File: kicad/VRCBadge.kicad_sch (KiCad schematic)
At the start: 0 parts

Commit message: feat: add power, peripheral schematics and custom component libraries
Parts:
- added C12, C17, C19, C20, C22: 100nF, symbol Device:C
- added C13, C14, C21: 1uF, symbol Device:C
- added C15, C16, C18: 10uF, symbol Device:C
- added D3, D4: LED_R, symbol Device:LED
- added J4: Conn_01x02, symbol Connector_Generic:Conn_01x02
- added J5: USB_C_Receptacle_USB2.0_16P, symbol Connector:USB_C_Receptacle_USB2.0_16P
- added J6: Conn_01x13_Socket, symbol Connector:Conn_01x13_Socket
- added Q2: FS8205A, Package_TO_SOT_SMD:SOT-23-6, symbol VRCBadge:FS8205A
- added R11, R12: 5.1k, symbol Device:R
- added R13, R14: 1k, symbol Device:R
- added R15: 1.2k, symbol Device:R
- added R16, R17, R18: 10k, symbol Device:R
- added R19, R20: 4.7k, symbol Device:R
- added SW3: RESET, symbol Switch:SW_Push
- added SW4: BOOT, symbol Switch:SW_Push
- added U10: MAX17048G+T10, VRCBadge:TDFN-8_L2.0-W2.0-P0.50-BL-EP1.2, symbol VRCBadge:MAX17048G+T10
- added U6: DW01A, Package_TO_SOT_SMD:SOT-23-6, symbol Battery_Management:DW01A
- added U7: ME6211C33M5, Package_TO_SOT_SMD:SOT-23-5, symbol Regulator_Linear:ME6211C33M5
- added U8: TP4056-42-ESOP8, Package_SO:SOIC-8-1EP_3.9x4.9mm_P1.27mm_EP2.41x3.3mm_ThermalVias, symbol Battery_Management:TP4056-42-ESOP8
- added U9: ESP32-S3-WROOM-1U, RF_Module:ESP32-S3-WROOM-1U, symbol RF_Module:ESP32-S3-WROOM-1
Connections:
- new net: J5.A5 (CC1), R12.1
- new net: J5.B5 (CC2), R11.1
- new net: D4.1 (K), R14.1
- new net: D4.2 (A), U8.6 (~{STDBY})
- new net: D3.1 (K), R13.1
- new net: D3.2 (A), U8.7 (~{CHRG})
- new net: C21.1, U10.1 (CTG)
- new net: C22.2, U10.3 (VDD)
- new net: R15.2, U8.2 (PROG)
- new net: Q2.2 (D), Q2.5 (D)
- new net: R16.2, U8.1 (TEMP)
- new net +3V3: C14.1, C18.1, C19.1, C20.1, C22.1, J6.13 (Pin_13), R17.1, R18.1, R19.1, R20.1, U10.2 (CELL), U7.5 (V_{OUT}), U9.2 (3V3)
- new net +BATT: C12.2, C13.1, C16.1, J4.1 (Pin_1), U6.5 (VCC), U7.1 (V_{IN}), U7.3 (CE), U8.5 (BAT)
- new net -BATT: J4.2 (Pin_2), Q2.3 (S)
- new net CS: C12.1, Q2.1 (S), U6.2 (CS), U6.6 (GND)
- new net ESP_BOOT: R18.2, SW4.2, U9.27 (IO0)
- new net ESP_EN: C17.1, R17.2, SW3.1, U9.3 (EN)
- new net GND: C13.2, C14.2, C15.2, C16.2, C17.2, C18.2, C19.2, C20.2, C21.2, J5.A1 (GND), J5.A12 (GND), J5.B1 (GND), J5.B12 (GND), J5.S1 (SHIELD), J6.12 (Pin_12), R11.2, R12.2, R15.1, R16.1, SW3.2, SW4.1, U10.4 (GND), U10.9 (EP), U7.2 (V_{SS}), U8.3 (GND), U8.9 (EPAD), U9.1 (GND), U9.40 (GND), U9.41 (GND)
- new net I2C_SCL: J6.3 (Pin_3), R19.2, U10.7 (SCL), U9.38 (IO2)
- new net I2C_SDA: J6.4 (Pin_4), R20.2, U10.8 (SDA), U9.39 (IO1)
- new net LCD_BL: J6.5 (Pin_5), U9.7 (IO7)
- new net LCD_CS: J6.8 (Pin_8), U9.18 (IO10)
- new net LCD_DC: J6.7 (Pin_7), U9.17 (IO9)
- new net LCD_MISO: J6.11 (Pin_11), U9.21 (IO13)
- new net LCD_MOSI: J6.10 (Pin_10), U9.19 (IO11)
- new net LCD_RST: J6.6 (Pin_6), U9.12 (IO8)
- new net LCD_SCLK: J6.9 (Pin_9), U9.20 (IO12)
- new net OC: Q2.4 (G), U6.3 (OC)
- new net OD: Q2.6 (G), U6.1 (OD)
- new net TP_INT: J6.2 (Pin_2), U9.15 (IO3)
- new net TP_RST: J6.1 (Pin_1), U9.4 (IO4)
- new net USB_DN: J5.A7 (D-), J5.B7 (D-), U9.13 (USB_D-)
- new net USB_DP: J5.A6 (D+), J5.B6 (D+), U9.14 (USB_D+)
- new net VBUS: C15.1, J5.A4 (VBUS), J5.A9 (VBUS), J5.B4 (VBUS), J5.B9 (VBUS), R13.2, R14.2, U8.4 (V_{CC}), U8.8 (CE)
- no-connect marks 0 -> 24
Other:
- added sheet mcu (mcu.kicad_sch)
- added sheet peripheral (peripheral.kicad_sch)
- added sheet power (power.kicad_sch)

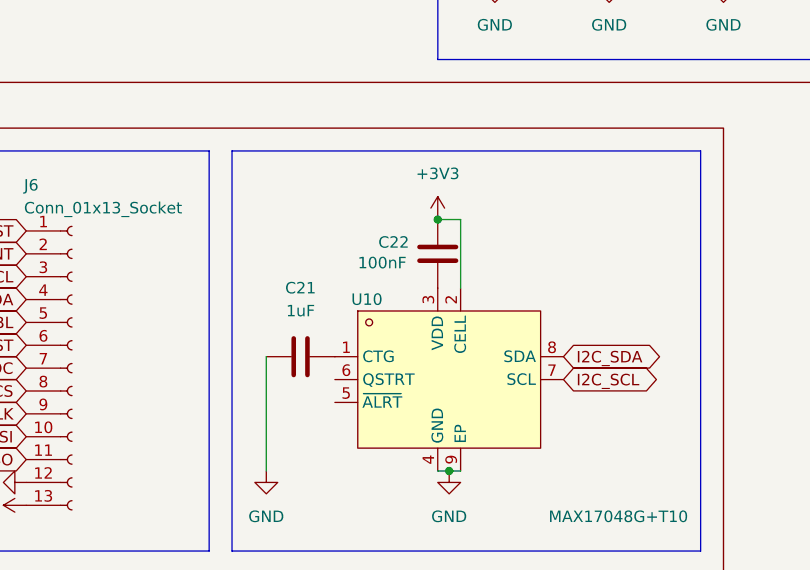
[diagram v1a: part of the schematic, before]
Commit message: feat: assign footprints and add no_connect flags for PCB readiness
- Assign footprints to 28 root-sheet components (0603 passives,
  0805 for 10uF, TL3342 switches, HRO USB-C, JST-PH/GH connectors)
- Add no_connect flags to MAX17048 ALRT and QSTRT pins
- Rewire MAX17048 CELL pin from +3V3 to +BATT on root sheet
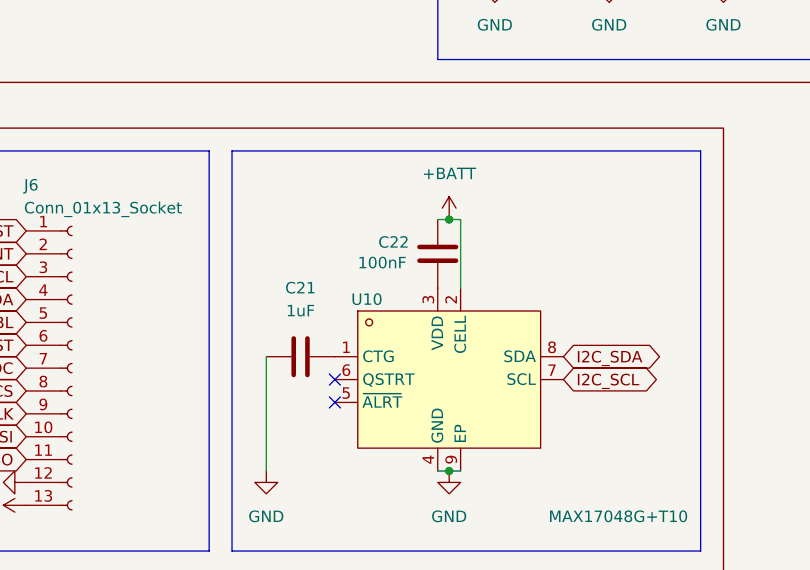
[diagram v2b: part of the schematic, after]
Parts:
- C12, C13, C14, C17, C19, C20, C21, C22: footprint (none) -> Capacitor_SMD:C_0603_1608Metric
- C15, C16, C18: footprint (none) -> Capacitor_SMD:C_0805_2012Metric
- D3, D4: footprint (none) -> LED_SMD:LED_0603_1608Metric
- J4: footprint (none) -> Connector_JST:JST_PH_S2B-PH-K_1x02_P2.00mm_Horizontal
- J5: footprint (none) -> Connector_USB:USB_C_Receptacle_HRO_TYPE-C-31-M-12
- J6: footprint (none) -> Connector_JST:JST_GH_SM13B-GHS-TB_1x13-1MP_P1.25mm_Horizontal
- R11, R12, R13, R14, R15, R16, R17, R18, R19, R20: footprint (none) -> Resistor_SMD:R_0603_1608Metric
- SW3, SW4: footprint (none) -> Button_Switch_SMD:SW_SPST_TL3342
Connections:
- net +3V3: no longer C22.1, U10.2 (CELL)
- net +BATT: now also C22.1, U10.2 (CELL)
- no-connect marks 24 -> 26
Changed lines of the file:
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@@
 	)
 	(junction
-		(at 255.27 147.32)
+		(at 256.54 147.32)
 		(diameter 0)
 		(color 0 0 0 0)
@@
 	)
 	(no_connect
+		(at 243.84 165.1)
+	)
+	(no_connect
 		(at 207.01 78.74)
 	)
@@
 	)
 	(no_connect
+		(at 243.84 167.64)
+	)
+	(no_connect
 		(at 237.49 55.88)
 	)
@@
 	(wire
 		(pts
+			(xy 256.54 147.32) (xy 255.27 147.32)
+		)
+		(stroke
+			(width 0)
+			(type default)
+		)
+	)
+	(wire
+		(pts
 			(xy 95.25 63.5) (xy 95.25 66.04)
 		)
@@
 	(wire
 		(pts
-			(xy 257.81 147.32) (xy 255.27 147.32)
+			(xy 257.81 147.32) (xy 256.54 147.32)
 		)
 		(stroke
@@
 			)
 		)
-		(property "Footprint" ""
+		(property "Footprint" "Resistor_SMD:R_0603_1608Metric"
 			(at 308.102 31.75 90)
 			(effects
@@
 			)
 		)
-		(property "Footprint" ""
+		(property "Footprint" "Connector_USB:USB_C_Receptacle_HRO_TYPE-C-31-M-12"
 			(at 39.37 45.72 0)
 			(effects
@@
 			)
 		)
-		(property "Footprint" ""
+		(property "Footprint" "Resistor_SMD:R_0603_1608Metric"
 			(at 64.262 41.91 90)
 			(effects
@@
 			)
 		)
-		(property "Footprint" ""
+		(property "Footprint" "LED_SMD:LED_0603_1608Metric"
 			(at 105.41 49.53 0)
 			(effects
@@
 			)
 		)
-		(property "Footprint" ""
+		(property "Footprint" "Connector_JST:JST_GH_SM13B-GHS-TB_1x13-1MP_P1.25mm_Horizontal"
 			(at 214.63 163.83 0)
 			(effects
@@
 			)
 		)
-		(property "Footprint" ""
+		(property "Footprint" "LED_SMD:LED_0603_1608Metric"
 			(at 95.25 49.53 0)
 			(effects
@@
 			)
 		)
-		(property "Footprint" ""
+		(property "Footprint" "Capacitor_SMD:C_0805_2012Metric"
 			(at 262.5852 120.65 0)
 			(effects
@@
 			)
 		)
-		(property "Footprint" ""
+		(property "Footprint" "Resistor_SMD:R_0603_1608Metric"
 			(at 316.992 31.75 90)
 			(effects
@@
 			)
 		)
-		(property "Footprint" ""
+		(property "Footprint" "Capacitor_SMD:C_0603_1608Metric"
 			(at 275.2852 93.98 0)
 			(effects
@@
 			)
 		)
-		(property "Footprint" ""
+		(property "Footprint" "Capacitor_SMD:C_0603_1608Metric"
 			(at 145.7452 101.6 0)
 			(effects
@@
 			)
 		)
-		(property "Footprint" ""
+		(property "Footprint" "Capacitor_SMD:C_0603_1608Metric"
 			(at 236.22 163.5252 0)
 			(effects
@@
 			)
 		)
-		(property "Footprint" ""
+		(property "Footprint" "Resistor_SMD:R_0603_1608Metric"
 			(at 142.748 49.53 90)
 			(effects
@@
 			)
 		)
-		(property "Footprint" ""
+		(property "Footprint" "Resistor_SMD:R_0603_1608Metric"
 			(at 71.882 41.91 90)
 			(effects
@@
 			)
 		)
-		(property "Footprint" ""
+		(property "Footprint" "Button_Switch_SMD:SW_SPST_TL3342"
 			(at 288.29 88.9 0)
 			(effects
@@
 			)
 		)
-		(property "Footprint" ""
+		(property "Footprint" "Capacitor_SMD:C_0603_1608Metric"
 			(at 256.2352 154.94 0)
 			(effects
@@
 			)
 		)
-		(property "Footprint" ""
+		(property "Footprint" "Connector_JST:JST_PH_S2B-PH-K_1x02_P2.00mm_Horizontal"
 			(at 24.13 92.71 0)
 			(effects
@@
 			)
 		)
-		(property "Footprint" ""
+		(property "Footprint" "Resistor_SMD:R_0603_1608Metric"
 			(at 275.082 33.02 90)
 			(effects
@@
 			)
 		)
-		(property "Footprint" ""
+		(property "Footprint" "Capacitor_SMD:C_0603_1608Metric"
 			(at 287.9852 120.65 0)
 			(effects
@@
 			)
 		)
-		(property "Footprint" ""
+		(property "Footprint" "Resistor_SMD:R_0603_1608Metric"
 			(at 272.542 74.93 90)
 			(effects
@@
 			)
 		)
-		(property "Footprint" ""
+		(property "Footprint" "Capacitor_SMD:C_0805_2012Metric"
 			(at 160.9852 52.07 0)
 			(effects
@@
 	)
 	(symbol
+		(lib_id "power:+BATT")
+		(at 256.54 147.32 0)
+		(unit 1)
+		(exclude_from_sim no)
+		(in_bom yes)
+		(on_board yes)
+		(dnp no)
+		(fields_autoplaced yes)
+		(property "Reference" "#PWR078"
+			(at 256.54 151.13 0)
+			(effects
+				(font
+					(size 1.27 1.27)
+				)
+				(hide yes)
+			)
+		)
+		(property "Value" "+BATT"
+			(at 256.54 142.24 0)
+			(effects
+				(font
+					(size 1.27 1.27)
+				)
+			)
+		)
+		(property "Footprint" ""
+			(at 256.54 147.32 0)
+			(effects
+				(font
+					(size 1.27 1.27)
+				)
+				(hide yes)
+			)
+		)
+		(property "Datasheet" ""
+			(at 256.54 147.32 0)
+			(effects
+				(font
+					(size 1.27 1.27)
+				)
+				(hide yes)
+			)
+		)
+		(property "Description" "Power symbol creates a global label with name \"+BATT\""
+			(at 256.54 147.32 0)
+			(effects
+				(font
+					(size 1.27 1.27)
+				)
+				(hide yes)
+			)
+		)
+		(pin "1"
+		)
+		(instances
+			(project ""
+				(path "/5848c585-af30-4d48-87e3-721d2ec71b1d"
+					(reference "#PWR078")
+					(unit 1)
+				)
+			)
+		)
+	)
+	(symbol
 		(lib_id "power:GND")
 		(at 171.45 52.07 0)
@@
 			)
 		)
-		(property "Footprint" ""
+		(property "Footprint" "Resistor_SMD:R_0603_1608Metric"
 			(at 93.472 59.69 90)
 			(effects
@@
 			)
 		)
-		(property "Footprint" ""
+		(property "Footprint" "Capacitor_SMD:C_0603_1608Metric"
 			(at 134.3152 101.6 0)
 			(effects
@@
 			)
 		)
-		(property "Footprint" ""
+		(property "Footprint" "Capacitor_SMD:C_0603_1608Metric"
 			(at 69.5452 137.16 0)
 			(effects
@@
 			)
 		)
-		(property "Footprint" ""
+		(property "Footprint" "Capacitor_SMD:C_0603_1608Metric"
 			(at 275.2852 120.65 0)
 			(effects
@@
 			)
 		)
-		(property "Footprint" ""
+		(property "Footprint" "Resistor_SMD:R_0603_1608Metric"
 			(at 150.368 49.53 90)
 			(effects
@@
 	)
 	(symbol
-		(lib_id "power:+3V3")
-		(at 255.27 147.32 0)
-		(unit 1)
-		(exclude_from_sim no)
-		(in_bom yes)
-		(on_board yes)
-		(dnp no)
-		(fields_autoplaced yes)
-		(property "Reference" "#PWR078"
-			(at 255.27 151.13 0)
-			(effects
-				(font
-					(size 1.27 1.27)
-				)
-				(hide yes)
-			)
-		)
-		(property "Value" "+3V3"
-			(at 255.27 142.24 0)
-			(effects
-				(font
-					(size 1.27 1.27)
-				)
-			)
-		)
-		(property "Footprint" ""
-			(at 255.27 147.32 0)
-			(effects
-				(font
-					(size 1.27 1.27)
-				)
-				(hide yes)
-			)
-		)
-		(property "Datasheet" ""
-			(at 255.27 147.32 0)
-			(effects
-				(font
-					(size 1.27 1.27)
-				)
-				(hide yes)
-			)
-		)
-		(property "Description" "Power symbol creates a global label with name \"+3V3\""
-			(at 255.27 147.32 0)
-			(effects
-				(font
-					(size 1.27 1.27)
-				)
-				(hide yes)
-			)
-		)
-		(pin "1"
-		)
-		(instances
-			(project "VRCBadge"
-				(path "/5848c585-af30-4d48-87e3-721d2ec71b1d"
-					(reference "#PWR078")
-					(unit 1)
-				)
-			)
-		)
-	)
-	(symbol
 		(lib_id "Regulator_Linear:ME6211C33M5")
 		(at 107.95 95.25 0)
@@
 			)
 		)
-		(property "Footprint" ""
+		(property "Footprint" "Resistor_SMD:R_0603_1608Metric"
 			(at 103.632 59.69 90)
 			(effects
@@
 			)
 		)
-		(property "Footprint" ""
+		(property "Footprint" "Button_Switch_SMD:SW_SPST_TL3342"
 			(at 289.56 45.72 0)
 			(effects
@@
 			)
 		)
-		(property "Footprint" ""
+		(property "Footprint" "Capacitor_SMD:C_0805_2012Metric"
 			(at 172.4152 52.07 0)
 			(effects

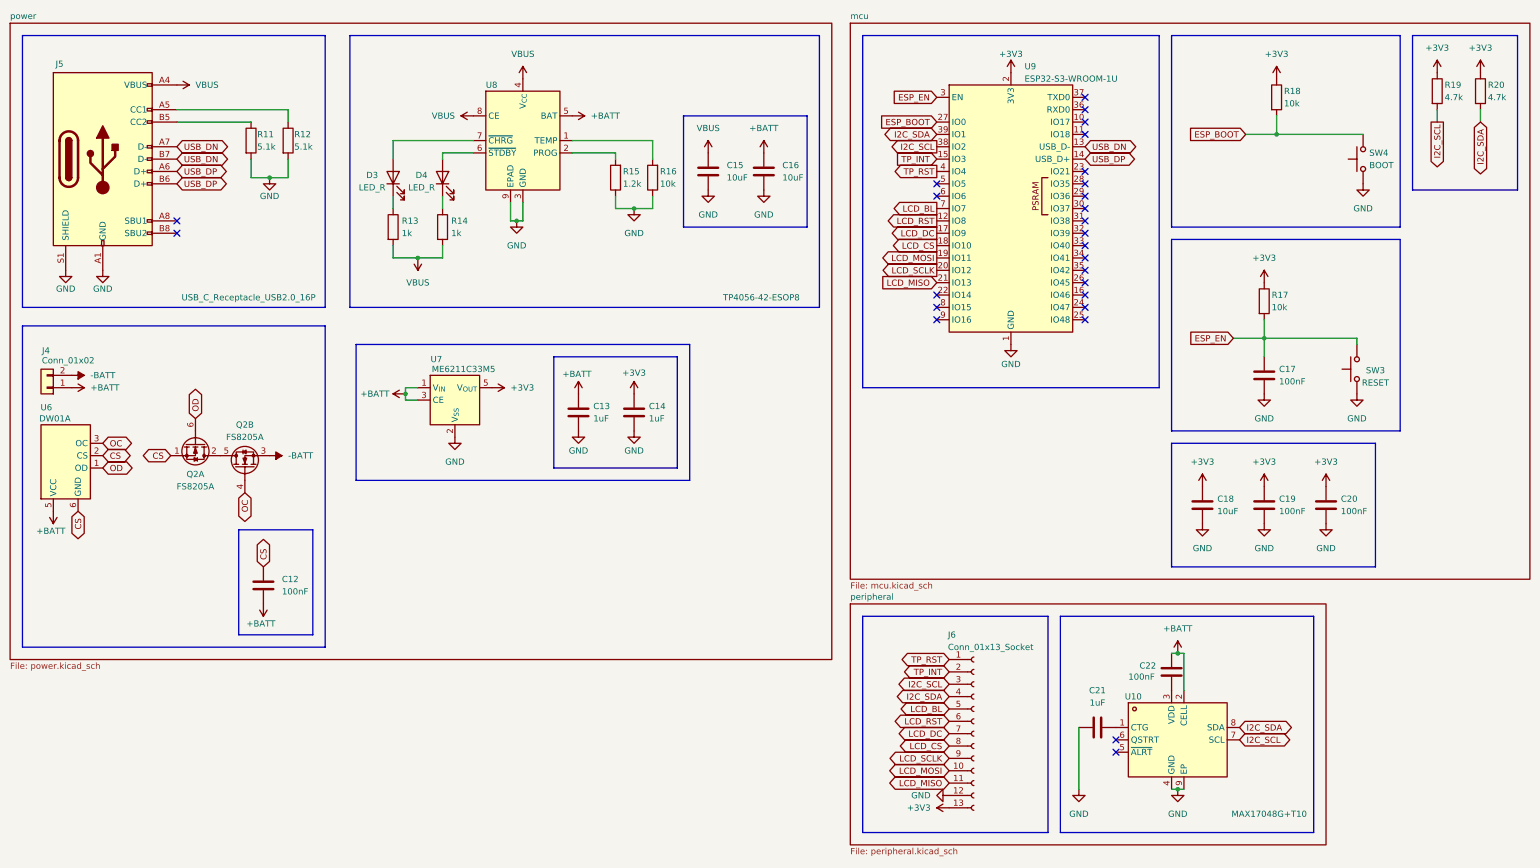
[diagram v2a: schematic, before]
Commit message: refactor: flatten schematic to single root sheet and fix ERC violations
- Remove hierarchical sub-sheets (power, mcu, peripheral) that
  duplicated root-sheet components and caused ERC conflicts
- Fix MAX17048 symbol pin types from unspecified to correct
  electrical types (power_in, bidirectional, input, passive, etc.)
- Sync DW01A lib_symbol with KiCad Battery_Management library
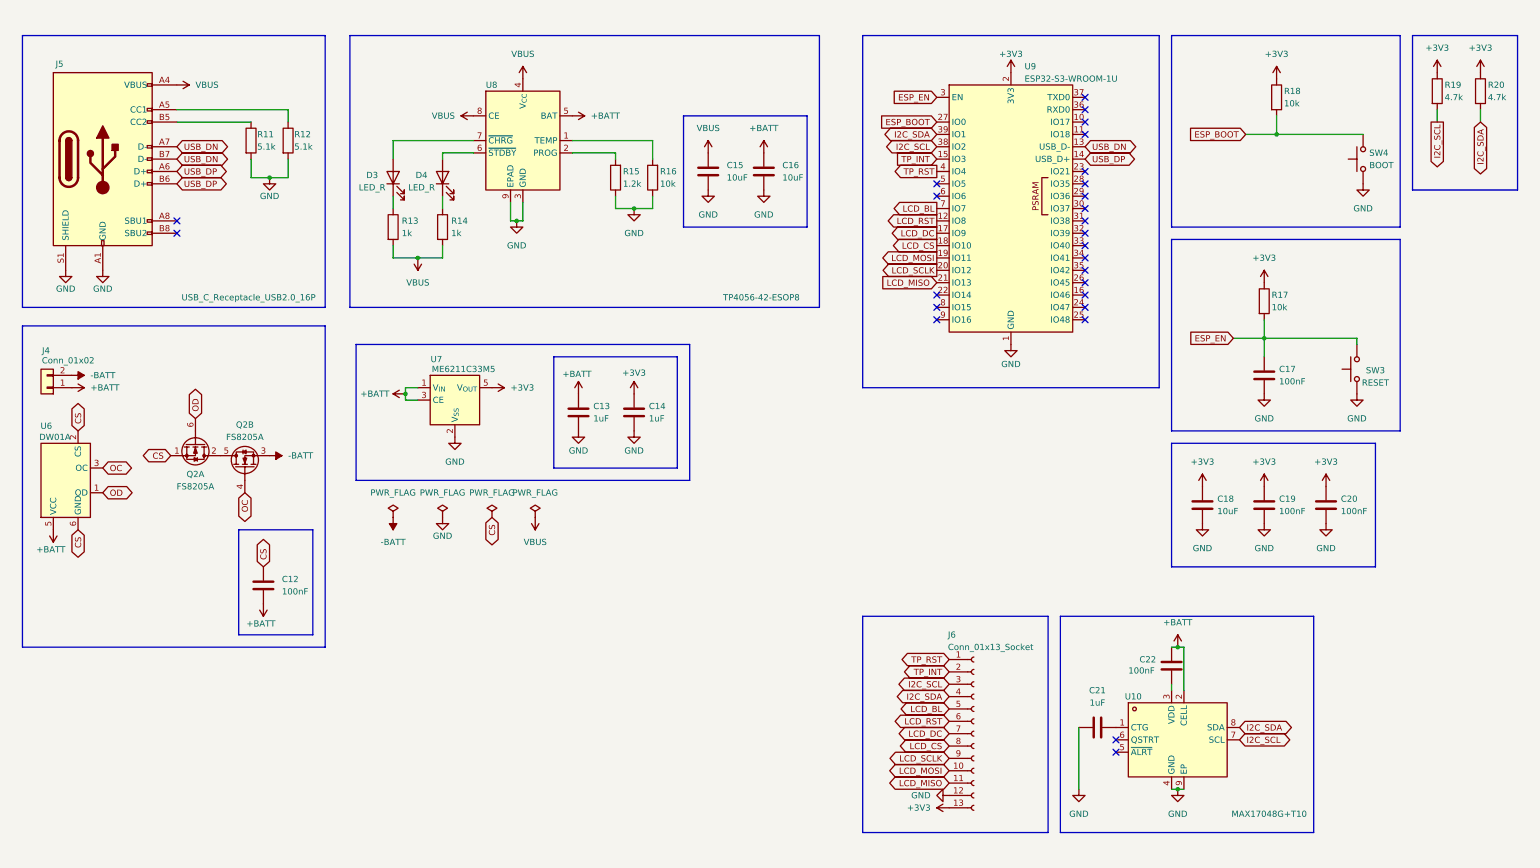
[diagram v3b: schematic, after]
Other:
- removed sheet mcu
- removed sheet peripheral
- removed sheet power
- moved on the sheet: C22, U6
